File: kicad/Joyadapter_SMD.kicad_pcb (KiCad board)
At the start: 2 copper layers, 47 x 37 mm, 16 parts, among them J1 AVR-ISP-6, J3 USB_B_Mini, U1 ATtiny4313-SU, X1 DB9_male, X2 DB9_male, Y1 12MHz

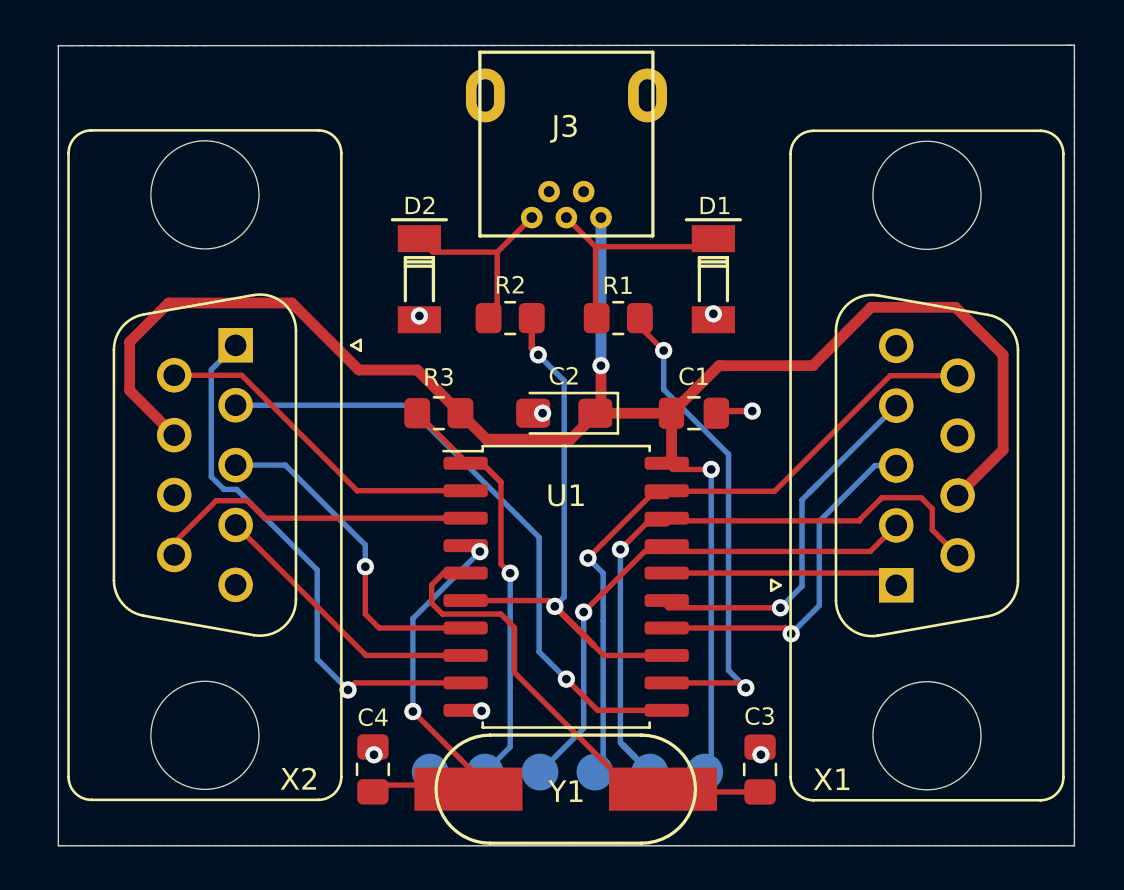
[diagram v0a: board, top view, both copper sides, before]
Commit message: Update
Fuse added
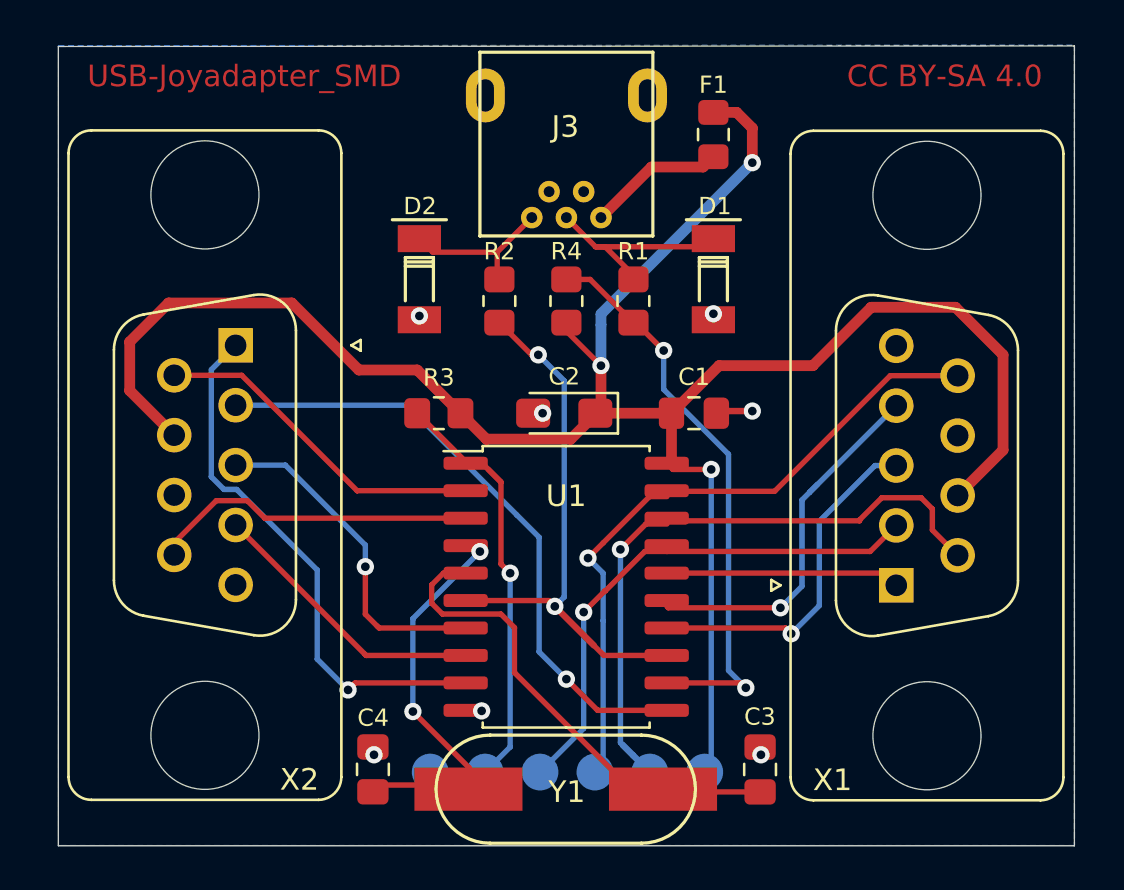
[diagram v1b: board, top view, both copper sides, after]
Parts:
- added F1: Fuse, Fuse:Fuse_0805_2012Metric_Pad1.15x1.40mm_HandSolder, F.Cu at (156.0, 92.4)
- added R4: 1.5k, Resistor_SMD:R_0805_2012Metric_Pad1.20x1.40mm_HandSolder, F.Cu at (149.2, 100.1)
- moved R1 1.06 mm to (152.3, 100.1), turned to 90 degrees
- moved R2 0.93 mm to (146.1, 100.1), turned to 90 degrees
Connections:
- J3 pad 1: VCC -> Net-(F1-Pad2)
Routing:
- net VCC: track 87.6 -> 99.4 mm, vias 2 -> 3
- net Net-(F1-Pad2): track 0.00 -> 6.37 mm
- net Net-(R1-Pad1): track 22.9 -> 26.8 mm
- net /D+: track 9.34 -> 7.42 mm
- net /D-: track 10.8 -> 9.81 mm
- net Net-(R2-Pad1): track 24.5 -> 25.1 mm

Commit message: Update PCB to V1.0
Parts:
- moved J3 0.34 mm to (149.2, 90.2)
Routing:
- net /D+: track 7.42 -> 9.57 mm
- net /D-: track 9.81 -> 10.2 mm, vias 0 -> 1
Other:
- board text added: "V1.0 - 06/21 - der-pw https://github.com/der-pw/USB-Joyadapter_SMD"
- board text removed: "V0.9 - 01/21 - der-pw https://github.com/der-pw/USB-Joyadapter_SMD"
